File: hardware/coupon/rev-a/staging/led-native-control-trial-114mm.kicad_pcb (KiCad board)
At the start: 6 copper layers, 114 x 32.5 mm, 483 parts, among them J1 USB4505-03-0-A, J2 S2B-PH-SM4-TB, SW1 EVQP7J01P, SW2 JS202011JCQN, U1 TLC59581RTQT, U11 SN74LVC1G04DBVR, U17 SN74LVC1G11DBVR, U2 74HC4514PW,118, U23 SN74LVC1G06DBVR, U24 SN74LVC2G17DBVR, U25 SN74LVC2G17DBVR, U29 TPS70933DBVR, U3 ESP32-S3-WROOM-1U-N16R8, U31 TUSB320LAIRWBR, U32 TS3USB31ERSER, U33 TPD4E05U06DQAR, U34 TPS3808G01DBVR, U35 MAX17048G+T10, U36 TPS631000DRLR, U37 TPS63020DSJT, U38 2.5V shunt, U39 TMP390A2DRLR, U40 SN74AUP1G125DBVR, U41 BQ24074RGTR, U42 SN74AUP1G125DBVR, U43 SN74AUP1G125DBVR, U44 TPS259474ARPWR, U45 TPS259474ARPWR, U46 TCA9517ADGKR, U47 TPS3823A-33DBVR, U48 SN74LVC1G04DSFR, U49 SN74LVC1G74RSER, U50 SN74LVC1G74RSER, U51 SN74LVC1G11DRYR, U52 SN74LVC1G08DSFR, U53 TLV6700DSER, U54 SN74LVC2G00DCUR, U55 SN74LVC2G08DCUR

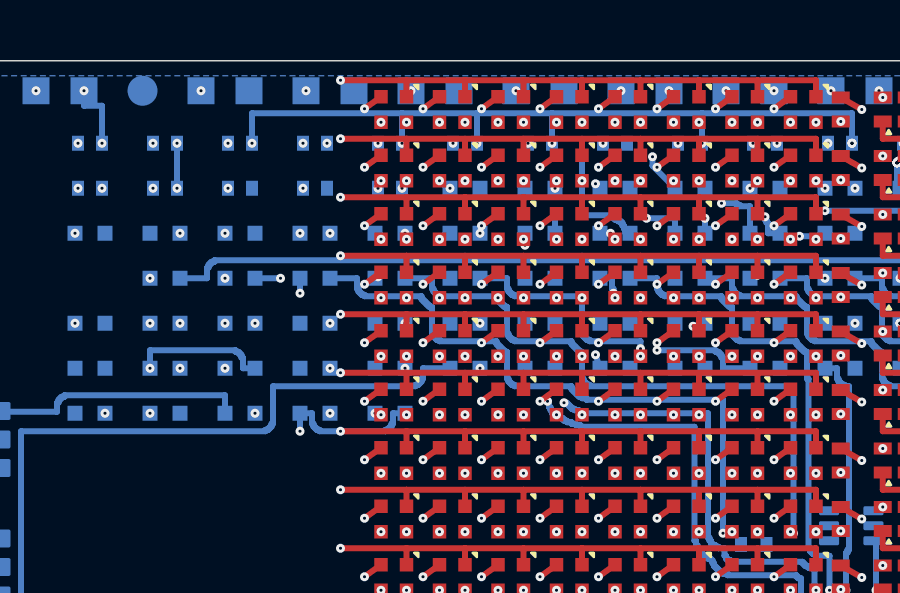
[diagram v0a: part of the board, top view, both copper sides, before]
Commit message: Extend reserved row-select detour to connect R29 ground
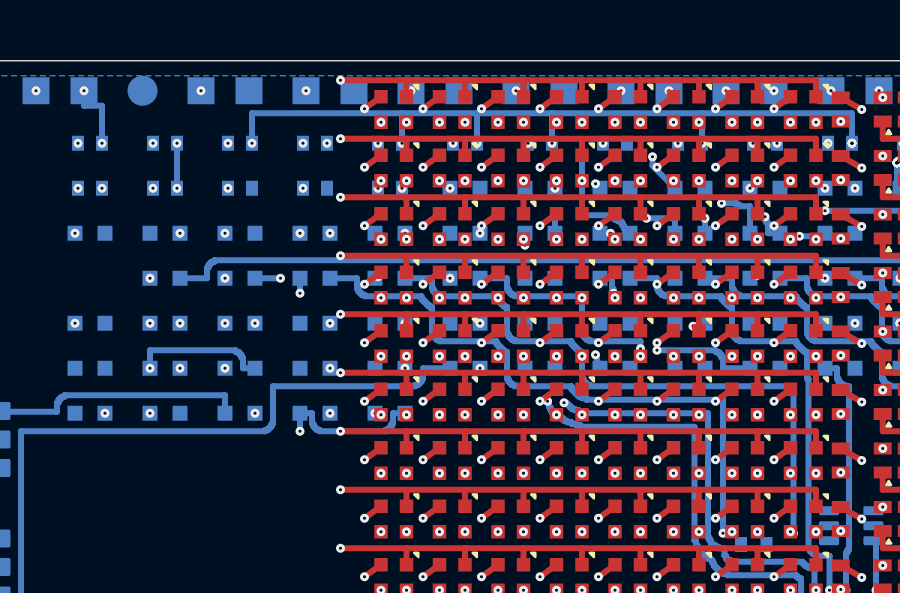
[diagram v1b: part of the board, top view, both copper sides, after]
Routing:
- net ROW_SEL_04: track 103.9 -> 102.9 mm, vias 13 -> 15
- net GND: vias 493 -> 496
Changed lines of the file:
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@@
 	)
 	(segment
-		(start 40.5 6.25)
-		(end 42.3 6.25)
+		(start 40.5 7.25)
+		(end 40.5 7.75)
 		(width 0.2)
-		(layer "In4.Cu")
+		(layer "In3.Cu")
 		(net "ROW_SEL_04")
 	)
 	(segment
-		(start 40.5 7.25)
-		(end 40.5 6.25)
+		(start 40.5 7.75)
+		(end 44.8 7.75)
 		(width 0.2)
-		(layer "In4.Cu")
+		(layer "In3.Cu")
 		(net "ROW_SEL_04")
 	)
@@
 	)
 	(segment
-		(start 42.3 6.25)
-		(end 42.3 7.25)
-		(width 0.2)
-		(layer "In4.Cu")
-		(net "ROW_SEL_04")
-	)
-	(segment
-		(start 42.3 7.25)
-		(end 54 7.25)
-		(width 0.2)
-		(layer "In4.Cu")
-		(net "ROW_SEL_04")
-	)
-	(segment
 		(start 42.35 11.75)
 		(end 42.35 12.1)
@@
 	)
 	(segment
+		(start 44.8 7.25)
+		(end 54 7.25)
+		(width 0.2)
+		(layer "In4.Cu")
+		(net "ROW_SEL_04")
+	)
+	(segment
+		(start 44.8 7.75)
+		(end 44.8 7.25)
+		(width 0.2)
+		(layer "In3.Cu")
+		(net "ROW_SEL_04")
+	)
+	(segment
 		(start 44.9 15.5)
 		(end 43.35 15.5)
@@
 	)
 	(via micro
+		(at 40.5 7.25)
+		(size 0.3)
+		(drill 0.1)
+		(layers "In3.Cu" "In4.Cu")
+		(net "ROW_SEL_04")
+	)
+	(via micro
 		(at 40.6 0.649999)
 		(size 0.3)
@@
 	)
 	(via micro
+		(at 44.25 7.25)
+		(size 0.3)
+		(drill 0.1)
+		(layers "In2.Cu" "In3.Cu")
+		(net "GND")
+	)
+	(via micro
+		(at 44.25 7.25)
+		(size 0.3)
+		(drill 0.1)
+		(layers "In3.Cu" "In4.Cu")
+		(net "GND")
+	)
+	(via micro
+		(at 44.25 7.25)
+		(size 0.3)
+		(drill 0.1)
+		(layers "In4.Cu" "B.Cu")
+		(net "GND")
+	)
+	(via micro
 		(at 44.35 2.3)
 		(size 0.3)
@@
 	)
 	(via micro
+		(at 44.8 7.25)
+		(size 0.3)
+		(drill 0.1)
+		(layers "In3.Cu" "In4.Cu")
+		(net "ROW_SEL_04")
+	)
+	(via micro

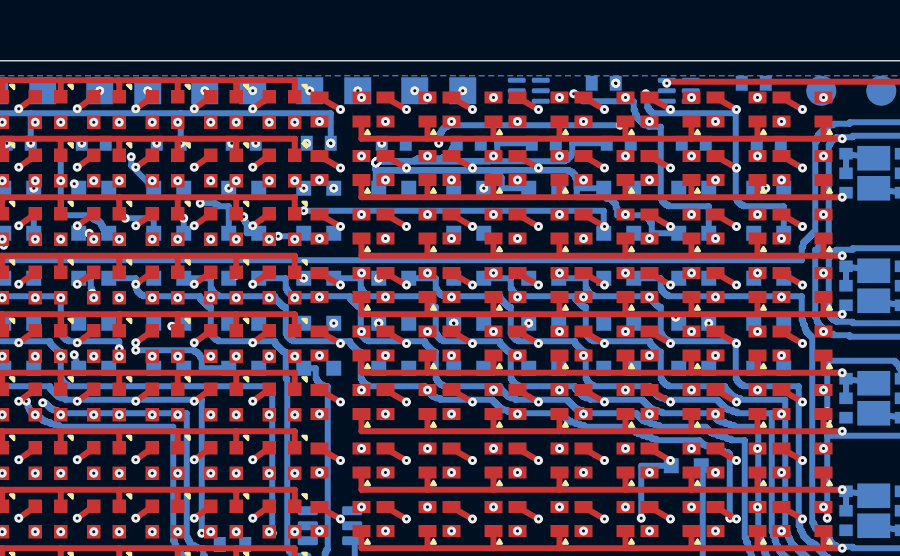
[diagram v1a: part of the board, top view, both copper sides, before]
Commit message: Reserve R2 ground with an offset colour-column detour
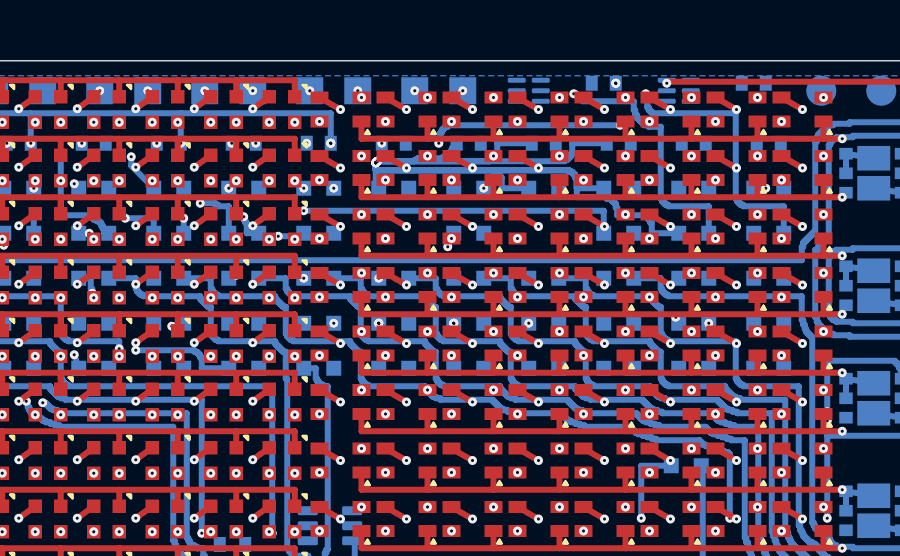
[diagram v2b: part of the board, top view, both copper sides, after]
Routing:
- net COL_07_R: track 55.6 -> 56.9 mm, vias 20 -> 22
- net GND: track 115.9 -> 116.4 mm, vias 496 -> 499
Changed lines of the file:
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@@
 	)
 	(segment
+		(start 60.2 6.05)
+		(end 56.45 6.05)
+		(width 0.2)
+		(layer "In4.Cu")
+		(net "COL_07_R")
+	)
+	(segment
+		(start 60.2 6.3)
+		(end 60.2 6.05)
+		(width 0.2)
+		(layer "In4.Cu")
+		(net "COL_07_R")
+	)
+	(segment
+		(start 60.2 6.7)
+		(end 60.2 6.3)
+		(width 0.2)
+		(layer "In3.Cu")
+		(net "COL_07_R")
+	)
+	(segment
 		(start 60.25 7.25)
 		(end 60.25 7.25)
@@
 	)
 	(segment
+		(start 61.75 5.75)
+		(end 61.55 6.2)
+		(width 0.2)
+		(layer "B.Cu")
+		(net "GND")
+	)
+	(segment
 		(start 61.75 8.75)
 		(end 61.75 14.05)
@@
 	)
 	(segment
+		(start 62.1 6.05)
+		(end 62.1 6.3)
+		(width 0.2)
+		(layer "In4.Cu")
+		(net "COL_07_R")
+	)
+	(segment
+		(start 62.1 6.3)
+		(end 62.1 6.7)
+		(width 0.2)
+		(layer "In3.Cu")
+		(net "COL_07_R")
+	)
+	(segment
+		(start 62.1 6.7)
+		(end 60.2 6.7)
+		(width 0.2)
+		(layer "In3.Cu")
+		(net "COL_07_R")
+	)
+	(segment
 		(start 62.2 12.05)
 		(end 62.2 12.1)
@@
 	(segment
 		(start 81.4 6.05)
-		(end 56.45 6.05)
+		(end 62.1 6.05)
 		(width 0.2)
 		(layer "In4.Cu")
@@
 	)
 	(via micro
+		(at 60.2 6.3)
+		(size 0.3)
+		(drill 0.1)
+		(layers "In3.Cu" "In4.Cu")
+		(net "COL_07_R")
+	)
+	(via micro
 		(at 60.45 1)
 		(size 0.3)
@@
 	)
 	(via micro
+		(at 61.55 6.2)
+		(size 0.3)
+		(drill 0.1)
+		(layers "In2.Cu" "In3.Cu")
+		(net "GND")
+	)
+	(via micro
+		(at 61.55 6.2)
+		(size 0.3)
+		(drill 0.1)
+		(layers "In3.Cu" "In4.Cu")
+		(net "GND")
+	)
+	(via micro
+		(at 61.55 6.2)
+		(size 0.3)
+		(drill 0.1)
+		(layers "In4.Cu" "B.Cu")
+		(net "GND")
+	)
+	(via micro
 		(at 61.675 11.775)
 		(size 0.3)
@@
 	)
 	(via micro
+		(at 62.1 6.3)
+		(size 0.3)
+		(drill 0.1)
+		(layers "In3.Cu" "In4.Cu")
+		(net "COL_07_R")
+	)
+	(via micro
